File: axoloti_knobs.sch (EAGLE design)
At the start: 18 parts, among them U1 JOYSTICKPTH

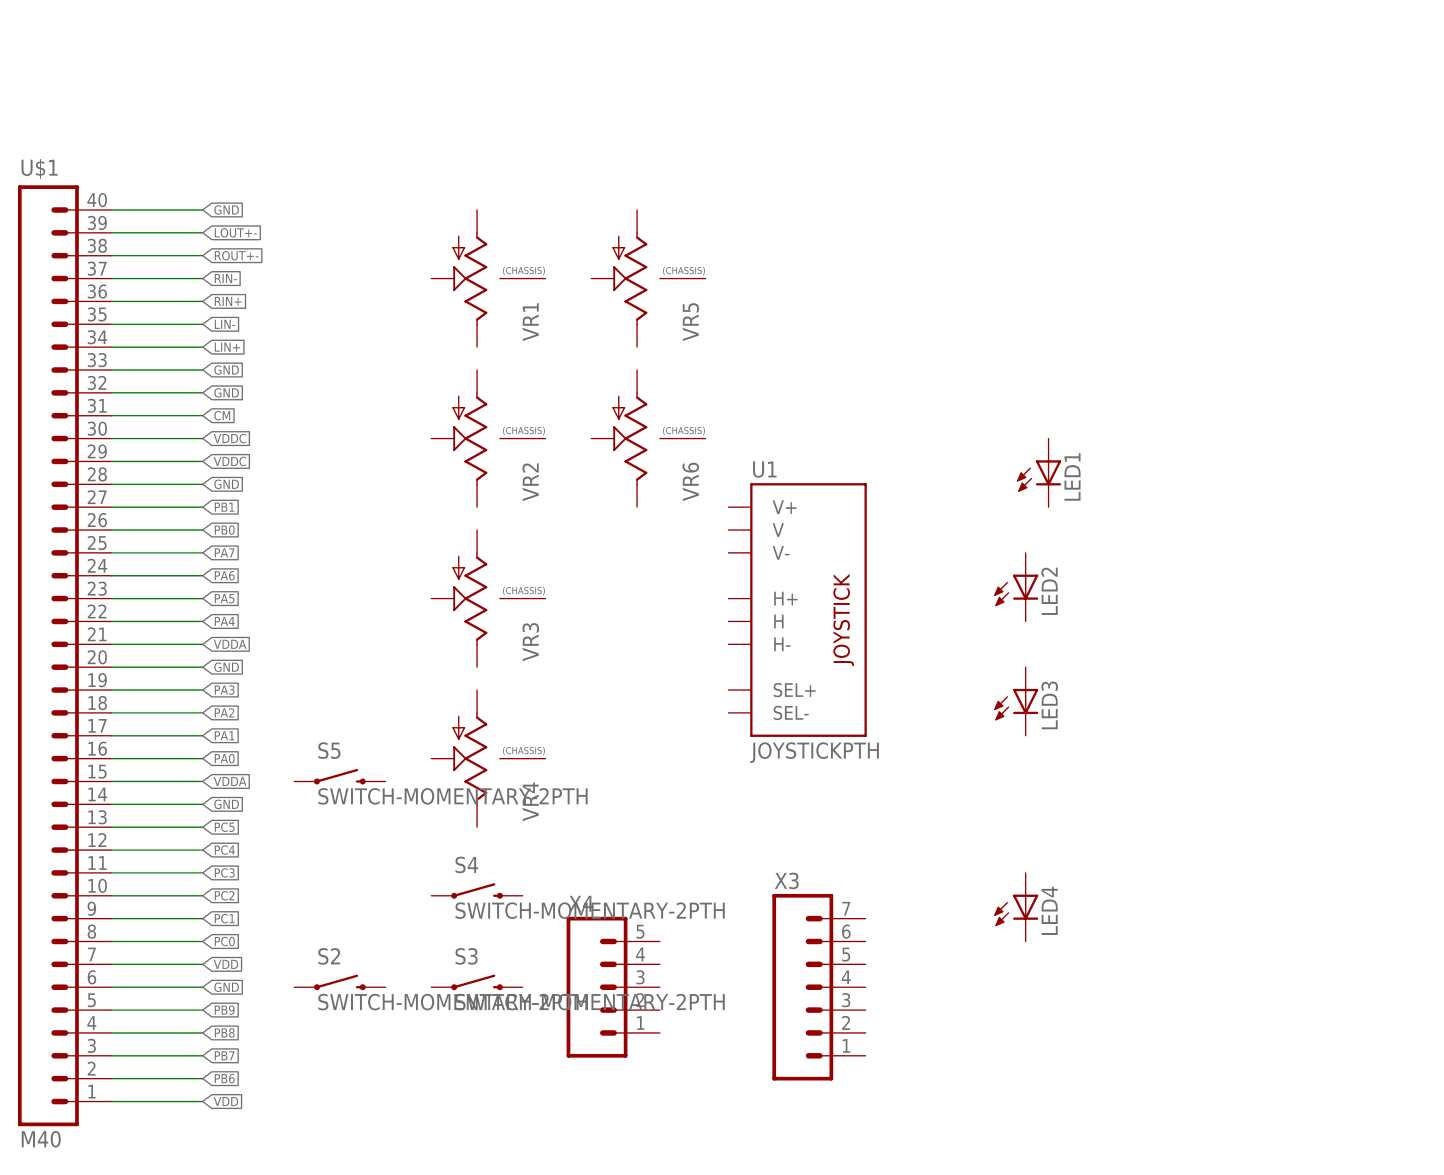
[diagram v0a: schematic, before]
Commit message: full width board
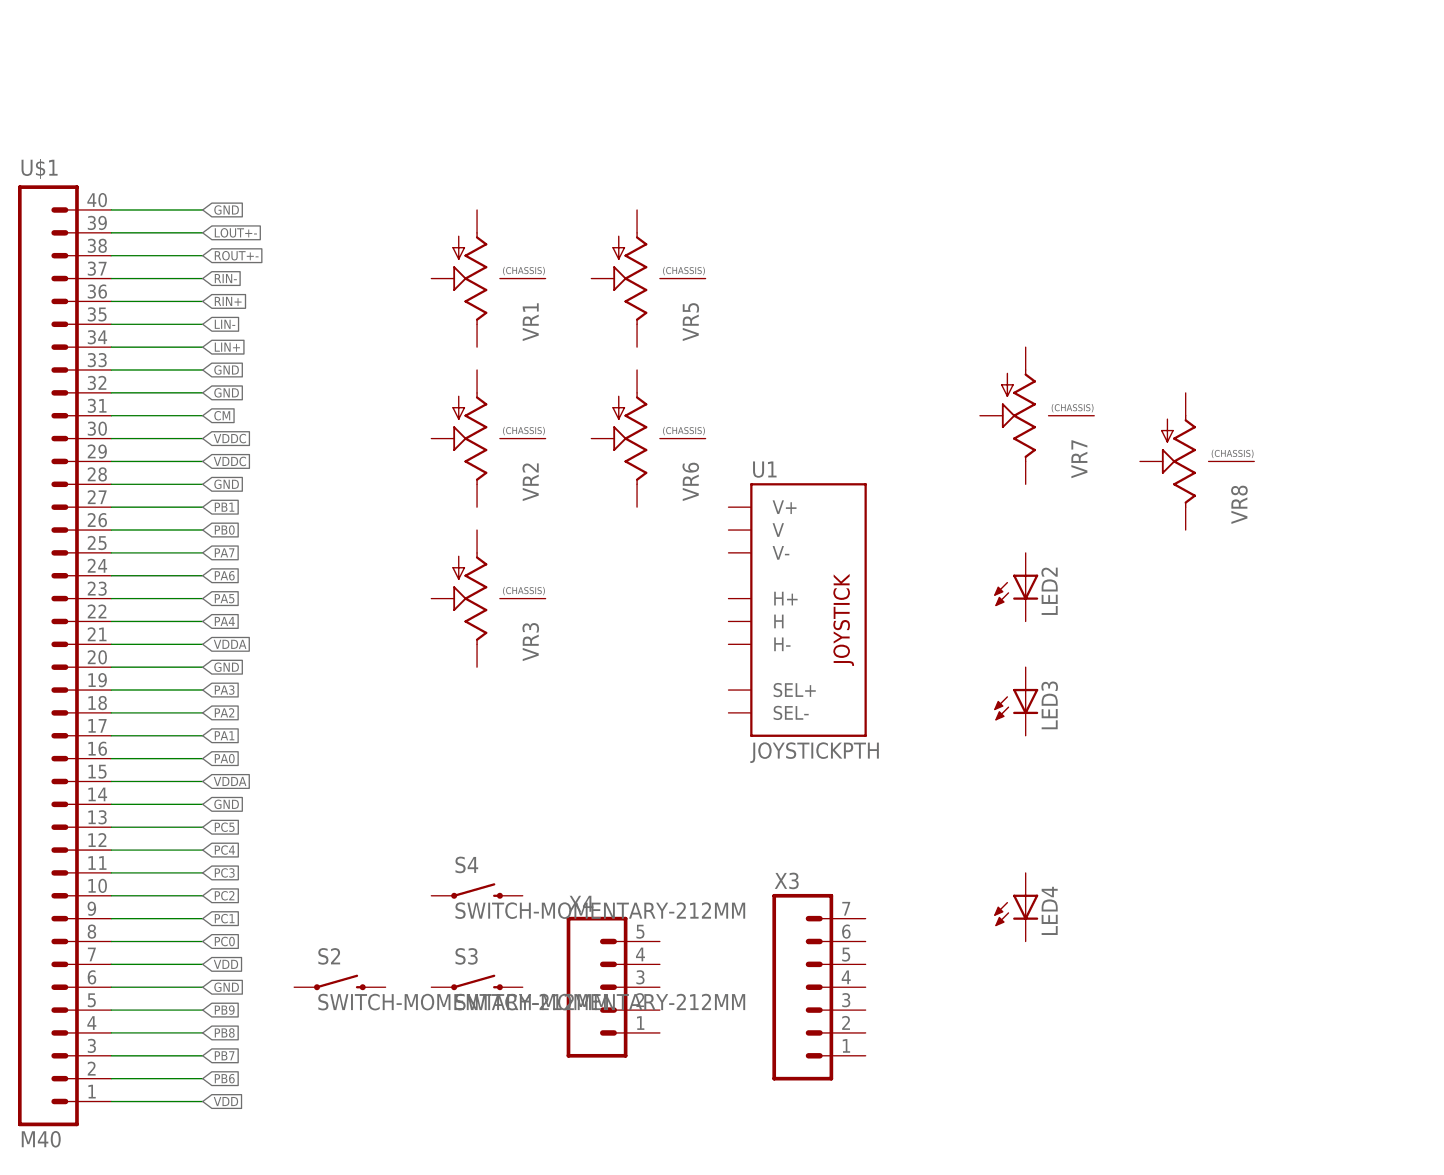
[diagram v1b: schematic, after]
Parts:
- removed LED1: (no value), SparkFun-LED:LED3MM
- removed S5: SWITCH-MOMENTARY-2PTH, SparkFun-Electromechanical:SWITCH-MOMENTARY-2PTH
- removed VR4: (no value), MusicThingModular:9MM_SNAP-IN_POT_CHASSIS
- added VR7, VR8: (no value), MusicThingModular:9MM_SNAP-IN_POT_CHASSIS
- S2, S3, S4: value SWITCH-MOMENTARY-2PTH -> SWITCH-MOMENTARY-212MM; device SparkFun-Electromechanical:SWITCH-MOMENTARY-2PTH -> SparkFun-Electromechanical:SWITCH-MOMENTARY-212MM
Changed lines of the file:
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@@
 <part name="VR2" library="MusicThingModular" deviceset="9MM_SNAP-IN_POT_CHASSIS" device=""/>
 <part name="VR3" library="MusicThingModular" deviceset="9MM_SNAP-IN_POT_CHASSIS" device=""/>
-<part name="VR4" library="MusicThingModular" deviceset="9MM_SNAP-IN_POT_CHASSIS" device=""/>
 <part name="VR5" library="MusicThingModular" deviceset="9MM_SNAP-IN_POT_CHASSIS" device=""/>
 <part name="VR6" library="MusicThingModular" deviceset="9MM_SNAP-IN_POT_CHASSIS" device=""/>
@@
 <part name="X4" library="SparkFun-Connectors" deviceset="M05" device="LOCK"/>
 <part name="X3" library="SparkFun-Connectors" deviceset="M07" device="LOCK"/>
-<part name="S2" library="SparkFun-Electromechanical" deviceset="SWITCH-MOMENTARY-2" device="PTH"/>
-<part name="S3" library="SparkFun-Electromechanical" deviceset="SWITCH-MOMENTARY-2" device="PTH"/>
-<part name="S4" library="SparkFun-Electromechanical" deviceset="SWITCH-MOMENTARY-2" device="PTH"/>
-<part name="S5" library="SparkFun-Electromechanical" deviceset="SWITCH-MOMENTARY-2" device="PTH"/>
-<part name="LED1" library="SparkFun-LED" deviceset="LED" device="3MM"/>
+<part name="S2" library="SparkFun-Electromechanical" deviceset="SWITCH-MOMENTARY-2" device="12MM" value="SWITCH-MOMENTARY-212MM"/>
+<part name="S3" library="SparkFun-Electromechanical" deviceset="SWITCH-MOMENTARY-2" device="12MM" value="SWITCH-MOMENTARY-212MM"/>
+<part name="S4" library="SparkFun-Electromechanical" deviceset="SWITCH-MOMENTARY-2" device="12MM" value="SWITCH-MOMENTARY-212MM"/>
 <part name="LED2" library="SparkFun-LED" deviceset="LED" device="3MM"/>
 <part name="LED3" library="SparkFun-LED" deviceset="LED" device="3MM"/>
 <part name="LED4" library="SparkFun-LED" deviceset="LED" device="3MM"/>
+<part name="VR7" library="MusicThingModular" deviceset="9MM_SNAP-IN_POT_CHASSIS" device=""/>
+<part name="VR8" library="MusicThingModular" deviceset="9MM_SNAP-IN_POT_CHASSIS" device=""/>
 </parts>
 <sheets>
@@
 <instance part="VR2" gate="G$1" x="63.5" y="81.28" rot="R180"/>
 <instance part="VR3" gate="G$1" x="63.5" y="63.5" rot="R180"/>
-<instance part="VR4" gate="G$1" x="63.5" y="45.72" rot="R180"/>
 <instance part="VR5" gate="G$1" x="81.28" y="99.06" rot="R180"/>
 <instance part="VR6" gate="G$1" x="81.28" y="81.28" rot="R180"/>
@@
 <instance part="S3" gate="G$1" x="63.5" y="20.32"/>
 <instance part="S4" gate="G$1" x="63.5" y="30.48"/>
-<instance part="S5" gate="G$1" x="48.26" y="43.18"/>
-<instance part="LED1" gate="G$1" x="127" y="78.74"/>
 <instance part="LED2" gate="G$1" x="124.46" y="66.04"/>
 <instance part="LED3" gate="G$1" x="124.46" y="53.34"/>
 <instance part="LED4" gate="G$1" x="124.46" y="30.48"/>
+<instance part="VR7" gate="G$1" x="124.46" y="83.82" rot="R180"/>
+<instance part="VR8" gate="G$1" x="142.24" y="78.74" rot="R180"/>
 </instances>
 <busses>

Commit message: wip
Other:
- note added: "Parts: B3F-4050 = 12mm square tactile switches B32-1310 = black keycap B32-1320 = orange B32-1330 = yellow B32-1360 = white B32-1380 = red 11mm spacer bolts"
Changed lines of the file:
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@@
 <sheet>
 <plain>
+<text x="106.68" y="106.68" size="1.778" layer="91">Parts:
+B3F-4050 = 12mm square tactile switches
+B32-1310 = black keycap
+B32-1320 = orange
+B32-1330 = yellow
+B32-1360 = white
+B32-1380 = red
+11mm spacer bolts </text>
 </plain>
 <instances>
@@
 </schematic>
 </drawing>
+<compatibility>
+<note version="6.3" minversion="6.2.2" severity="warning">
+Since Version 6.2.2 text objects can contain more than one line,
+which will not be processed correctly with this version.
+</note>
+</compatibility>
 </eagle>
